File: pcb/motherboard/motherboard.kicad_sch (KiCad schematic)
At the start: 30 parts, among them J3 UART_USB, J4 I2C_HEADER, J6 SPI_TEST, SW2 GEN_MAZE, SW3 TOGGLE_MAZE, SW4 SOLVE_MAZE, U2 CH340C, U6 PCA9306D

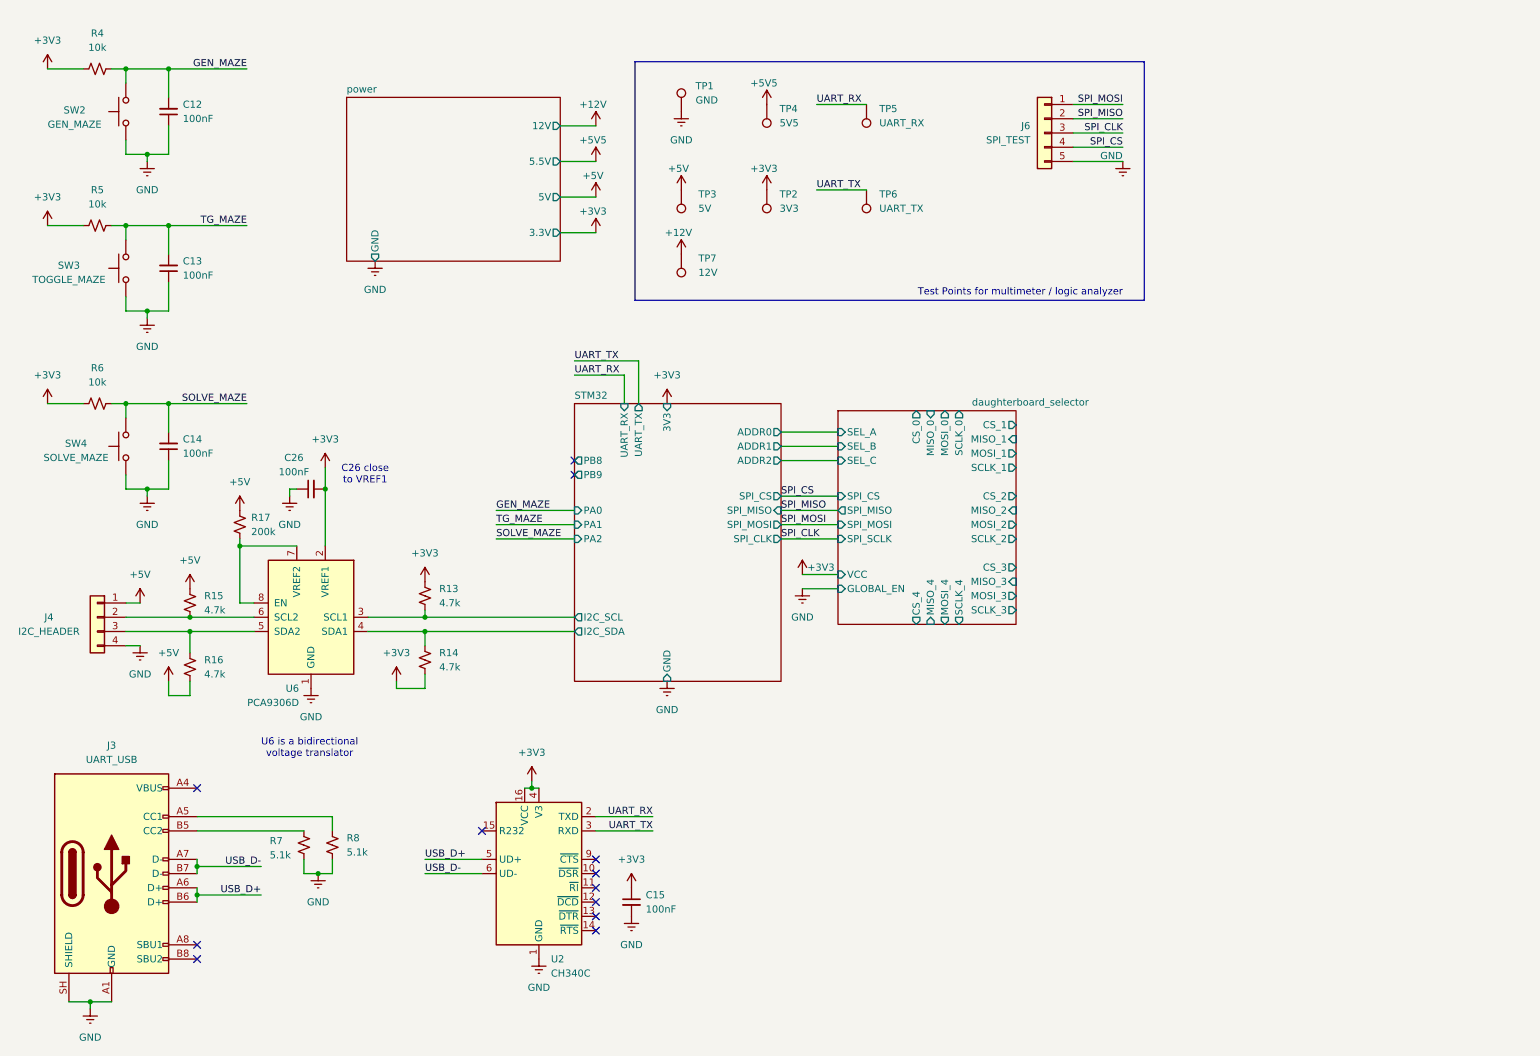
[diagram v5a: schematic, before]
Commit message: added daughterboard sockets to motherboard
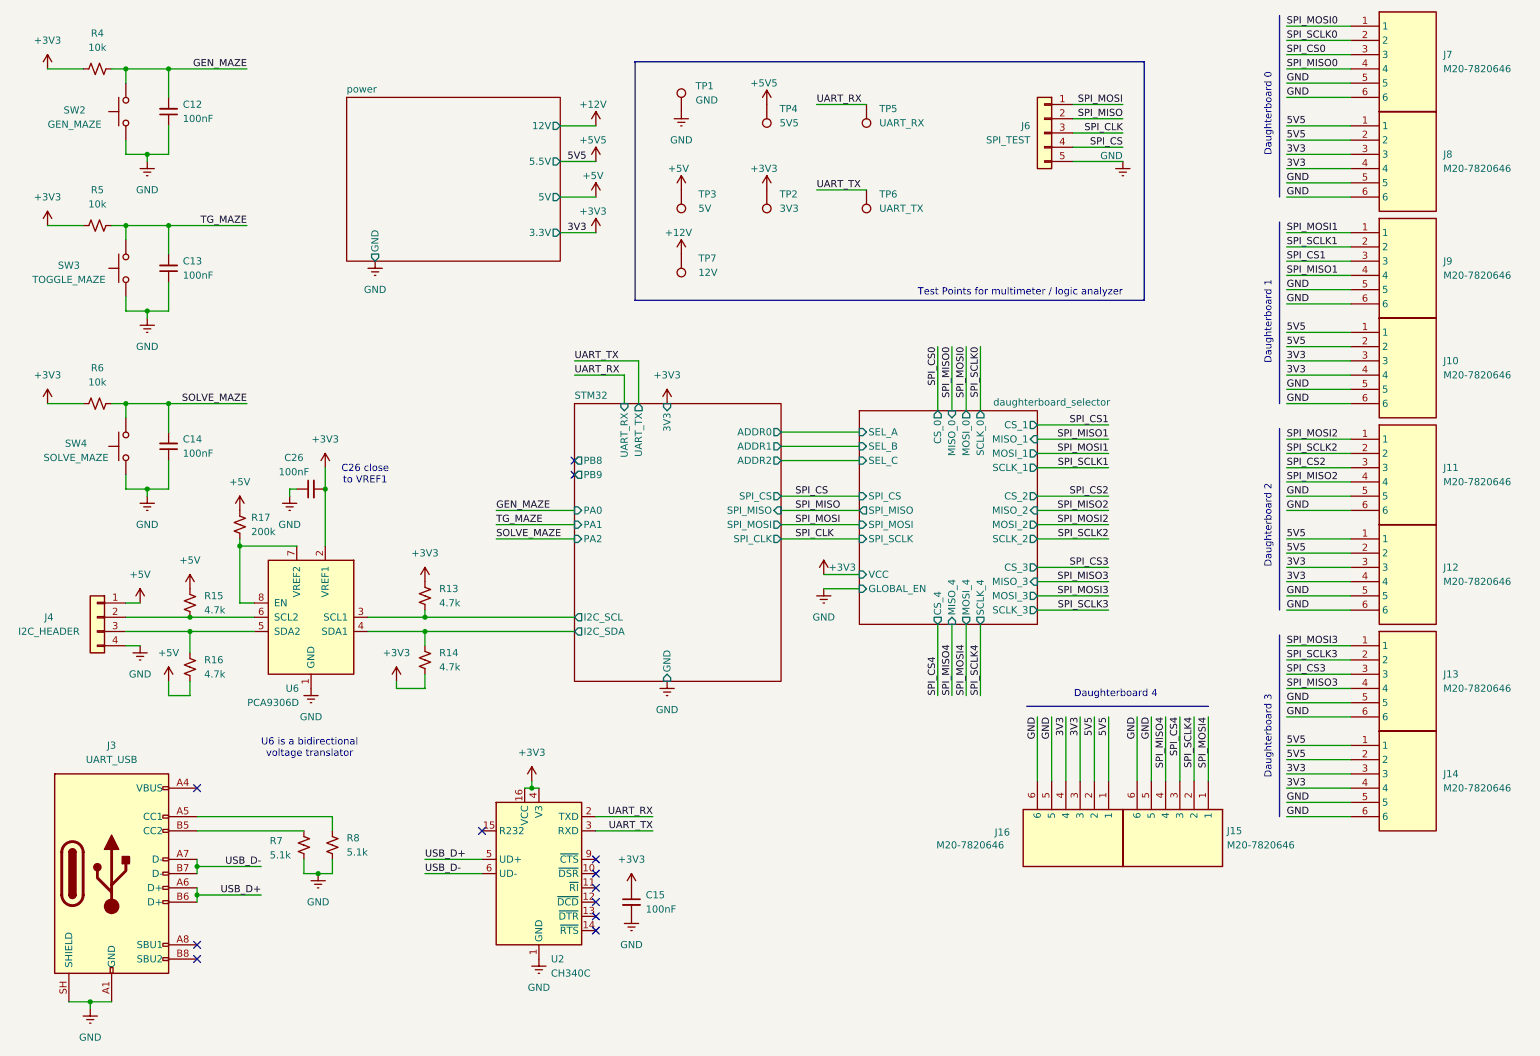
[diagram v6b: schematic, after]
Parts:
- added J10, J11, J12, J13, J14, J15, J16, J7, J8, J9: M20-7820646, HDRV6W70P0X254_1X6_1564X250X850P, symbol KiCad:M20-7820646
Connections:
- net +3V3: now also J10.3, J10.4, J12.3, J12.4, J14.3, J14.4, J16.3, J16.4, J8.3, J8.4
- net +5V5: now also J10.1, J10.2, J12.1, J12.2, J14.1, J14.2, J16.1, J16.2, J8.1, J8.2
- net GND: now also J10.5, J10.6, J11.5, J11.6, J12.5, J12.6, J13.5, J13.6, J14.5, J14.6, J15.5, J15.6, J16.5, J16.6, J7.5, J7.6, J8.5, J8.6, J9.5, J9.6
- new net SPI_CS0: J7.3
- new net SPI_CS1: J9.3
- new net SPI_CS2: J11.3
- new net SPI_CS3: J13.3
- new net SPI_CS4: J15.3
- new net SPI_MISO0: J7.4
- new net SPI_MISO1: J9.4
- new net SPI_MISO2: J11.4
- new net SPI_MISO3: J13.4
- new net SPI_MISO4: J15.4
- new net SPI_MOSI0: J7.1
- new net SPI_MOSI1: J9.1
- new net SPI_MOSI2: J11.1
- new net SPI_MOSI3: J13.1
- new net SPI_MOSI4: J15.1
- new net SPI_SCLK0: J7.2
- new net SPI_SCLK1: J9.2
- new net SPI_SCLK2: J11.2
- new net SPI_SCLK3: J13.2
- new net SPI_SCLK4: J15.2
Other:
- note added: "Daughterboard 0"
- note added: "Daughterboard 1"
- note added: "Daughterboard 2"
- note added: "Daughterboard 3"
- note added: "Daughterboard 4"

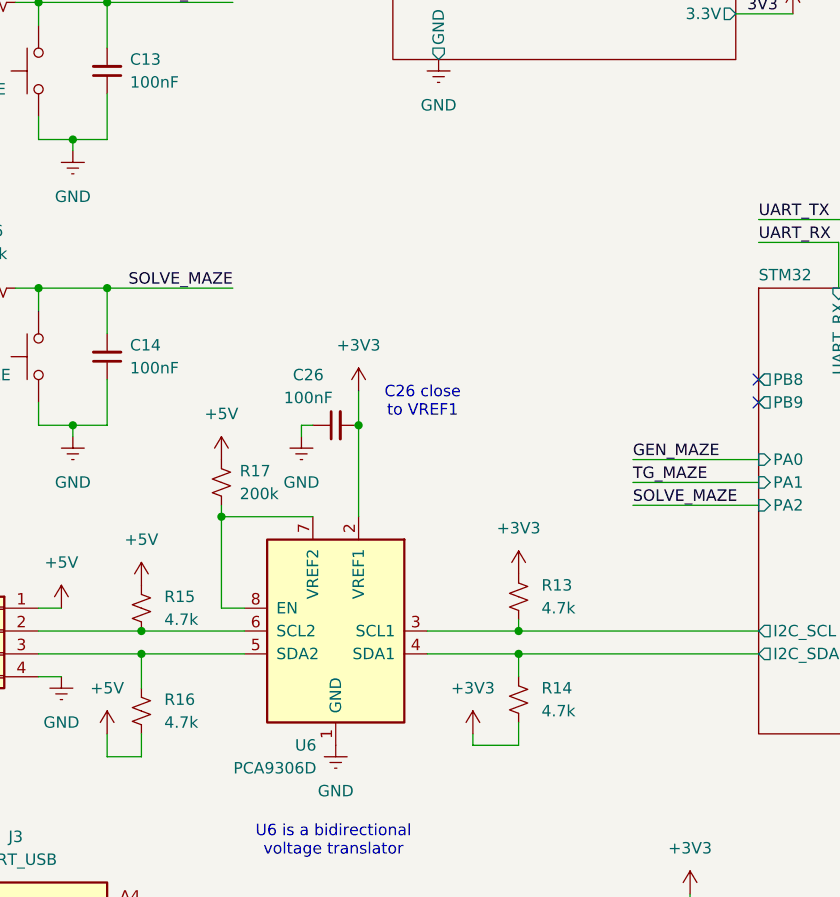
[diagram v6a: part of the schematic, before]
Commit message: consolidated BOM for motherboard, added terminal blocks for external motors
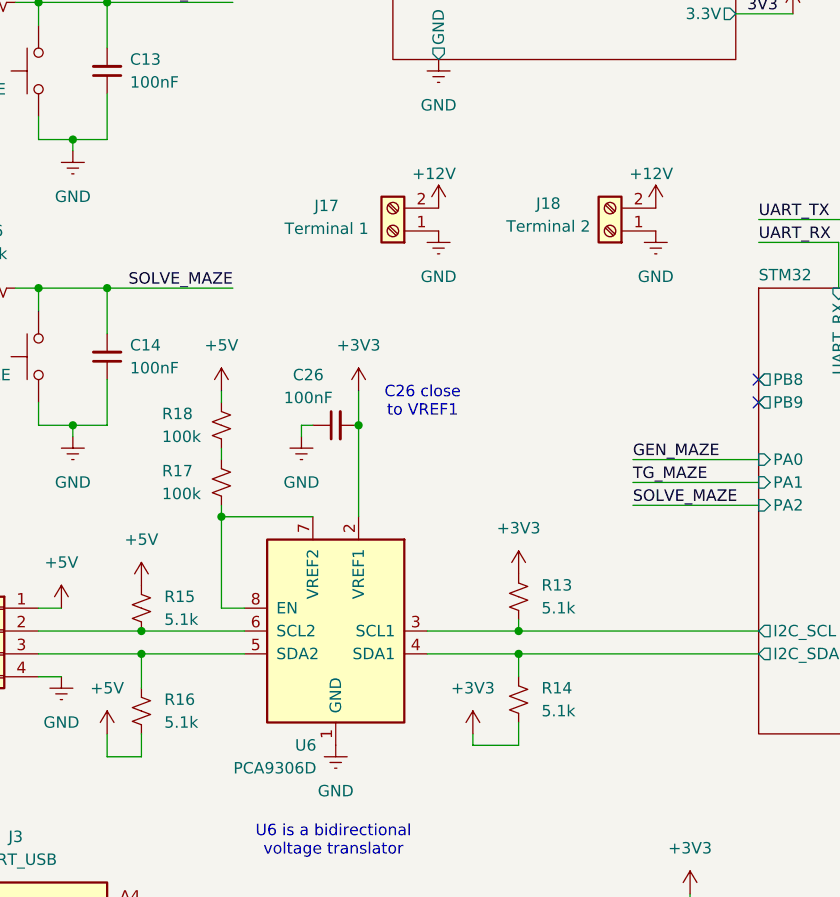
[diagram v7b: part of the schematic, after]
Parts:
- added J17: Terminal 1, TerminalBlock_Phoenix:TerminalBlock_Phoenix_MKDS-1,5-2-5.08_1x02_P5.08mm_Horizontal, symbol Connector:Screw_Terminal_01x02
- added J18: Terminal 2, TerminalBlock_Phoenix:TerminalBlock_Phoenix_MKDS-1,5-2-5.08_1x02_P5.08mm_Horizontal, symbol Connector:Screw_Terminal_01x02
- added R18: 100k, Resistor_SMD:R_0603_1608Metric, symbol Device:R_Small_US
- J10, J11, J12, J13, J14, J15, J16, J7, J8, J9: footprint HDRV6W70P0X254_1X6_1564X250X850P -> KiCad:HDRV6W70P0X254_1X6_1564X250X850P
- R13, R14, R15, R16: value 4.7k -> 5.1k
- R17: value 200k -> 100k
- TP1, TP2, TP3, TP4, TP5, TP6, TP7: now left out of the parts list
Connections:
- net +12V: now also J17.2 (Pin_2), J18.2 (Pin_2)
- net +5V: now also R18.1; no longer R17.1
- net GND: now also J17.1 (Pin_1), J18.1 (Pin_1)
- new net: R17.1, R18.2

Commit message: added 3d models for remaining components
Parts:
- added H1, H2, H3, H4: MountingHole, MountingHole:MountingHole_4.3mm_M4, symbol Mechanical:MountingHole
